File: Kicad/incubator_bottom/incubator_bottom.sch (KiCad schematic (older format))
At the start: 37 parts, among them J1 Conn_01x02, J2 Conn_02x03_Odd_Even, J3 RJ12, J4 Conn_01x05, J5 AudioJack3_SwitchTR, J6 AudioJack3_SwitchTR, J7 Conn_01x02, J8 Conn_01x06, Q1 ZXMS6004, Q2 IPB80N03S4L-03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

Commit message: fix: Power resistor size
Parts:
- removed H5, H6, H7, H8: MountingHole, MountingHole:MountingHole_4.3mm_M4, symbol incubator_bottom-rescue:MountingHole-Mechanical
- removed R7: HSC1004R0J, Incubator:HSC1004R0J, symbol Incubator:HSC1004R0J
- added R?: HSC1004R0J, Incubator:100W4RJ, symbol Incubator:HSC1004R0J
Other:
- note removed: "FAN HOLES"
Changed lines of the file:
@@
 NoConn ~ 7650 1475
-$Comp
-L incubator_bottom-rescue:MountingHole-Mechanical H5
-U 1 1 6110AD0D
-P 5025 7225
-F 0 "H5" H 5125 7271 50  0000 L CNN
-F 1 "MountingHole" H 5125 7180 50  0000 L CNN
-F 2 "MountingHole:MountingHole_4.3mm_M4" H 5025 7225 50  0001 C CNN
-F 3 "~" H 5025 7225 50  0001 C CNN
-	1    5025 7225
-	1    0    0    -1
-$EndComp
-$Comp
-L incubator_bottom-rescue:MountingHole-Mechanical H7
-U 1 1 6110B26F
-P 5800 7225
-F 0 "H7" H 5900 7271 50  0000 L CNN
-F 1 "MountingHole" H 5900 7180 50  0000 L CNN
-F 2 "MountingHole:MountingHole_4.3mm_M4" H 5800 7225 50  0001 C CNN
-F 3 "~" H 5800 7225 50  0001 C CNN
-	1    5800 7225
-	1    0    0    -1
-$EndComp
-$Comp
-L incubator_bottom-rescue:MountingHole-Mechanical H6
-U 1 1 6110B9C7
-P 5025 7500
-F 0 "H6" H 5125 7546 50  0000 L CNN
-F 1 "MountingHole" H 5125 7455 50  0000 L CNN
-F 2 "MountingHole:MountingHole_4.3mm_M4" H 5025 7500 50  0001 C CNN
-F 3 "~" H 5025 7500 50  0001 C CNN
-	1    5025 7500
-	1    0    0    -1
-$EndComp
-$Comp
-L incubator_bottom-rescue:MountingHole-Mechanical H8
-U 1 1 6110BE5B
-P 5800 7475
-F 0 "H8" H 5900 7521 50  0000 L CNN
-F 1 "MountingHole" H 5900 7430 50  0000 L CNN
-F 2 "MountingHole:MountingHole_4.3mm_M4" H 5800 7475 50  0001 C CNN
-F 3 "~" H 5800 7475 50  0001 C CNN
-	1    5800 7475
-	1    0    0    -1
-$EndComp
 $Comp
 L incubator_bottom-rescue:+12V-power #PWR0105
@@
 Text Notes 3600 7000 0    50   ~ 0
 EXTERNAL HOLES
-Text Notes 5500 7000 0    50   ~ 0
-FAN HOLES
 Text Notes 4675 6850 0    102  ~ 0
 HOLES
@@
 Wire Notes Line
 	475  3325 5925 3325
-$Comp
-L Incubator:HSC1004R0J R7
-U 1 1 610E9CE6
-P 8475 5300
-F 0 "R7" H 8545 5346 50  0000 L CNN
-F 1 "HSC1004R0J" H 8545 5255 50  0000 L CNN
-F 2 "Incubator:HSC1004R0J" V 8405 5300 50  0001 C CNN
-F 3 "https://www.mouser.com/datasheet/2/418/5/ENG_CD_1625999_AH2-1990035.pdf" H 8475 5300 50  0001 C CNN
-	1    8475 5300
-	1    0    0    -1
-$EndComp
-NoConn ~ 8475 5150
-NoConn ~ 8475 5450
+NoConn ~ 7700 5150
+NoConn ~ 7700 5450
 $Comp
 L incubator_bottom-rescue:C-Device C3
@@
 Text Notes 3250 5275 0    102  ~ 0
 PID
+$Comp
+L Incubator:HSC1004R0J R?
+U 1 1 6141DEAF
+P 7700 5300
+F 0 "R?" H 7770 5346 50  0000 L CNN
+F 1 "HSC1004R0J" H 7770 5255 50  0000 L CNN
+F 2 "Incubator:100W4RJ" V 7630 5300 50  0001 C CNN
+F 3 "https://www.mouser.com/datasheet/2/418/5/ENG_CD_1625999_AH2-1990035.pdf" H 7700 5300 50  0001 C CNN
+	1    7700 5300
+	1    0    0    -1
+$EndComp
 $EndSCHEMATC

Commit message: fix: Power resistor size and position
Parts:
- removed R?: HSC1004R0J, Incubator:100W4RJ, symbol Incubator:HSC1004R0J
- added R15, R7: 100W4RJ, Incubator:100W4RJ, symbol Incubator:HSC1004R0J
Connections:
- no-connect marks 8 -> 10
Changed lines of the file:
@@
 PID
 $Comp
-L Incubator:HSC1004R0J R?
-U 1 1 6141DEAF
+L Incubator:HSC1004R0J R15
+U 1 1 61434FDD
+P 6450 5250
+F 0 "R15" H 6520 5296 50  0000 L CNN
+F 1 "100W4RJ" H 6520 5205 50  0000 L CNN
+F 2 "Incubator:100W4RJ" V 6380 5250 50  0001 C CNN
+F 3 "https://www.mouser.com/datasheet/2/418/5/ENG_CD_1625999_AH2-1990035.pdf" H 6450 5250 50  0001 C CNN
+	1    6450 5250
+	1    0    0    -1
+$EndComp
+$Comp
+L Incubator:HSC1004R0J R7
+U 1 1 61442D39
 P 7700 5300
-F 0 "R?" H 7770 5346 50  0000 L CNN
-F 1 "HSC1004R0J" H 7770 5255 50  0000 L CNN
+F 0 "R7" H 7770 5346 50  0000 L CNN
+F 1 "100W4RJ" H 7770 5255 50  0000 L CNN
 F 2 "Incubator:100W4RJ" V 7630 5300 50  0001 C CNN
 F 3 "https://www.mouser.com/datasheet/2/418/5/ENG_CD_1625999_AH2-1990035.pdf" H 7700 5300 50  0001 C CNN
@@
 	1    0    0    -1
 $EndComp
+NoConn ~ 6450 5100
+NoConn ~ 6450 5400
 $EndSCHEMATC

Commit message: fix: fan connection
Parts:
- removed J4: Conn_01x05, Connector_PinHeader_2.54mm:PinHeader_1x05_P2.54mm_Vertical, symbol incubator_bottom-rescue:Conn_01x05-Connector_Generic
- removed R15: 100W4RJ, Incubator:100W4RJ, symbol Incubator:HSC1004R0J
- added H5, H6, H7, H8: MountingHole, MountingHole:MountingHole_3.2mm_M3, symbol incubator_bottom-rescue:MountingHole-Mechanical
- added J10, J11, J4, J9: Conn_01x01, Connector_Wire:SolderWirePad_1x01_SMD_5x10mm, symbol Connector_Generic:Conn_01x01
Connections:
- no-connect marks 10 -> 8
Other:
- note added: "FAN HOLES"
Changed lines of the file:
@@
 	1    0    0    -1
 $EndComp
-Text GLabel 4950 3925 0    50   Input ~ 0
+Text GLabel 4950 3900 0    50   Input ~ 0
 12V
-Wire Wire Line
-	5125 3925 5050 3925
-Wire Wire Line
-	5050 3925 5050 3850
 $Comp
 L incubator_bottom-rescue:GND-power #PWR0102
 U 1 1 611DACB0
-P 5050 4400
-F 0 "#PWR0102" H 5050 4150 50  0001 C CNN
-F 1 "GND" H 5055 4227 50  0000 C CNN
-F 2 "" H 5050 4400 50  0001 C CNN
-F 3 "" H 5050 4400 50  0001 C CNN
-	1    5050 4400
-	1    0    0    -1
-$EndComp
-Wire Wire Line
-	5125 4125 5050 4125
-Wire Wire Line
-	5050 4125 5050 4400
-Text GLabel 4950 4225 0    50   Input ~ 0
+P 5050 4450
+F 0 "#PWR0102" H 5050 4200 50  0001 C CNN
+F 1 "GND" H 5055 4277 50  0000 C CNN
+F 2 "" H 5050 4450 50  0001 C CNN
+F 3 "" H 5050 4450 50  0001 C CNN
+	1    5050 4450
+	1    0    0    -1
+$EndComp
+Text GLabel 4950 4200 0    50   Input ~ 0
 SDA
-Text GLabel 4950 4325 0    50   Input ~ 0
+Text GLabel 4950 4350 0    50   Input ~ 0
 SCL
-Wire Wire Line
-	5125 4325 4950 4325
-Wire Wire Line
-	4950 4225 5125 4225
 $Comp
 L incubator_bottom-rescue:AudioJack3_SwitchTR-Connector J5
@@
 L incubator_bottom-rescue:+12V-power #PWR0105
 U 1 1 6111A394
-P 5050 3850
-F 0 "#PWR0105" H 5050 3700 50  0001 C CNN
-F 1 "+12V" H 5065 4023 50  0000 C CNN
-F 2 "" H 5050 3850 50  0001 C CNN
-F 3 "" H 5050 3850 50  0001 C CNN
-	1    5050 3850
-	1    0    0    -1
-$EndComp
-Wire Wire Line
-	4950 3925 5050 3925
-Connection ~ 5050 3925
+P 5050 3800
+F 0 "#PWR0105" H 5050 3650 50  0001 C CNN
+F 1 "+12V" H 5065 3973 50  0000 C CNN
+F 2 "" H 5050 3800 50  0001 C CNN
+F 3 "" H 5050 3800 50  0001 C CNN
+	1    5050 3800
+	1    0    0    -1
+$EndComp
 $Comp
 L incubator_bottom-rescue:+12V-power #PWR0108
@@
 Text Notes 1950 5250 0    102  ~ 0
 FAN
-$Comp
-L incubator_bottom-rescue:Conn_01x05-Connector_Generic J4
-U 1 1 6118C3B2
-P 5325 4125
-F 0 "J4" H 5405 4167 50  0000 L CNN
-F 1 "Conn_01x05" H 5405 4076 50  0000 L CNN
-F 2 "Connector_PinHeader_2.54mm:PinHeader_1x05_P2.54mm_Vertical" H 5325 4125 50  0001 C CNN
-F 3 "~" H 5325 4125 50  0001 C CNN
-	1    5325 4125
-	1    0    0    -1
-$EndComp
 Text GLabel 4750 1025 2    50   Input ~ 0
 C0
@@
 PID
 $Comp
-L Incubator:HSC1004R0J R15
-U 1 1 61434FDD
-P 6450 5250
-F 0 "R15" H 6520 5296 50  0000 L CNN
-F 1 "100W4RJ" H 6520 5205 50  0000 L CNN
-F 2 "Incubator:100W4RJ" V 6380 5250 50  0001 C CNN
-F 3 "https://www.mouser.com/datasheet/2/418/5/ENG_CD_1625999_AH2-1990035.pdf" H 6450 5250 50  0001 C CNN
-	1    6450 5250
-	1    0    0    -1
-$EndComp
-$Comp
 L Incubator:HSC1004R0J R7
 U 1 1 61442D39
@@
 	1    0    0    -1
 $EndComp
-NoConn ~ 6450 5100
-NoConn ~ 6450 5400
+$Comp
+L Connector_Generic:Conn_01x01 J4
+U 1 1 61426717
+P 5350 3900
+F 0 "J4" H 5430 3942 50  0000 L CNN
+F 1 "Conn_01x01" H 5430 3851 50  0000 L CNN
+F 2 "Connector_Wire:SolderWirePad_1x01_SMD_5x10mm" H 5350 3900 50  0001 C CNN
+F 3 "~" H 5350 3900 50  0001 C CNN
+	1    5350 3900
+	1    0    0    -1
+$EndComp
+$Comp
+L Connector_Generic:Conn_01x01 J11
+U 1 1 614274D6
+P 5350 4350
+F 0 "J11" H 5430 4392 50  0000 L CNN
+F 1 "Conn_01x01" H 5430 4301 50  0000 L CNN
+F 2 "Connector_Wire:SolderWirePad_1x01_SMD_5x10mm" H 5350 4350 50  0001 C CNN
+F 3 "~" H 5350 4350 50  0001 C CNN
+	1    5350 4350
+	1    0    0    -1
+$EndComp
+Wire Wire Line
+	4950 3900 5050 3900
+Wire Wire Line
+	5050 3800 5050 3900
+Connection ~ 5050 3900
+Wire Wire Line
+	5050 3900 5150 3900
+Wire Wire Line
+	5150 4050 5050 4050
+$Comp
+L Connector_Generic:Conn_01x01 J10
+U 1 1 61427056
+P 5350 4200
+F 0 "J10" H 5430 4242 50  0000 L CNN
+F 1 "Conn_01x01" H 5430 4151 50  0000 L CNN
+F 2 "Connector_Wire:SolderWirePad_1x01_SMD_5x10mm" H 5350 4200 50  0001 C CNN
+F 3 "~" H 5350 4200 50  0001 C CNN
+	1    5350 4200
+	1    0    0    -1
+$EndComp
+$Comp
+L Connector_Generic:Conn_01x01 J9
+U 1 1 61426C44
+P 5350 4050
+F 0 "J9" H 5430 4092 50  0000 L CNN
+F 1 "Conn_01x01" H 5430 4001 50  0000 L CNN
+F 2 "Connector_Wire:SolderWirePad_1x01_SMD_5x10mm" H 5350 4050 50  0001 C CNN
+F 3 "~" H 5350 4050 50  0001 C CNN
+	1    5350 4050
+	1    0    0    -1
+$EndComp
+Wire Wire Line
+	5050 4450 5050 4050
+Wire Wire Line
+	4950 4200 5150 4200
+Wire Wire Line
+	5150 4350 4950 4350
+$Comp
+L incubator_bottom-rescue:MountingHole-Mechanical H5
+U 1 1 614A8308
+P 5000 7150
+F 0 "H5" H 5100 7196 50  0000 L CNN
+F 1 "MountingHole" H 5100 7105 50  0000 L CNN
+F 2 "MountingHole:MountingHole_3.2mm_M3" H 5000 7150 50  0001 C CNN
+F 3 "~" H 5000 7150 50  0001 C CNN
+	1    5000 7150
+	1    0    0    -1
+$EndComp
+$Comp
+L incubator_bottom-rescue:MountingHole-Mechanical H6
+U 1 1 614A89BD
+P 5000 7450
+F 0 "H6" H 5100 7496 50  0000 L CNN
+F 1 "MountingHole" H 5100 7405 50  0000 L CNN
+F 2 "MountingHole:MountingHole_3.2mm_M3" H 5000 7450 50  0001 C CNN
+F 3 "~" H 5000 7450 50  0001 C CNN
+	1    5000 7450
+	1    0    0    -1
+$EndComp
+$Comp
+L incubator_bottom-rescue:MountingHole-Mechanical H7
+U 1 1 614A8DD5
+P 5800 7150
+F 0 "H7" H 5900 7196 50  0000 L CNN
+F 1 "MountingHole" H 5900 7105 50  0000 L CNN
+F 2 "MountingHole:MountingHole_3.2mm_M3" H 5800 7150 50  0001 C CNN
+F 3 "~" H 5800 7150 50  0001 C CNN
+	1    5800 7150
+	1    0    0    -1
+$EndComp
+$Comp
+L incubator_bottom-rescue:MountingHole-Mechanical H8
+U 1 1 614A963E
+P 5800 7450
+F 0 "H8" H 5900 7496 50  0000 L CNN
+F 1 "MountingHole" H 5900 7405 50  0000 L CNN
+F 2 "MountingHole:MountingHole_3.2mm_M3" H 5800 7450 50  0001 C CNN
+F 3 "~" H 5800 7450 50  0001 C CNN
+	1    5800 7450
+	1    0    0    -1
+$EndComp
+Text Notes 5250 7000 0    50   ~ 0
+FAN HOLES
 $EndSCHEMATC

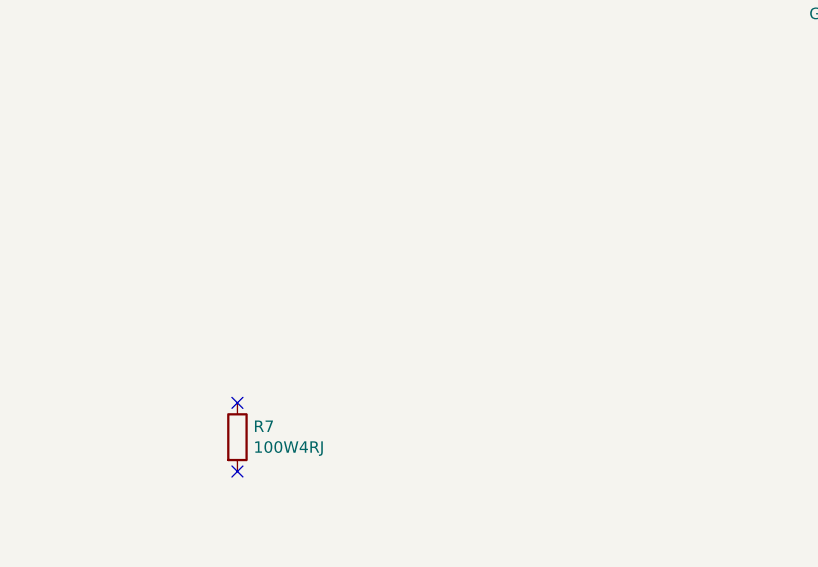
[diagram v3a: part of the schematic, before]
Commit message: refactor:Step-down IC was changed
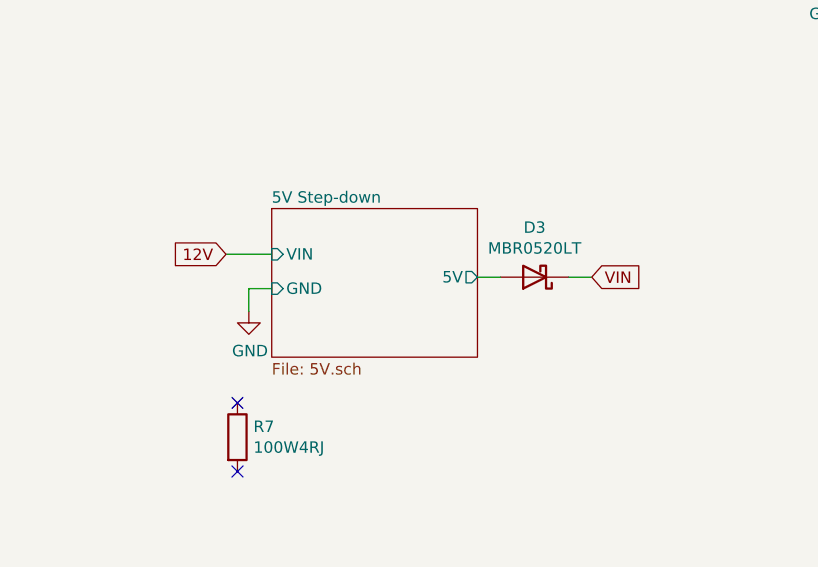
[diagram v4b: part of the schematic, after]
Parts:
- added D3: MBR0520LT, Diode_SMD:D_SOD-123, symbol incubator_bottom-rescue:MBR0520LT-Diode
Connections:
- net VIN: now also D3.1 (K)
- new net 5V Step-down/5V: D3.2 (A)
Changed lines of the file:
@@
 $Descr A4 11693 8268
 encoding utf-8
-Sheet 1 2
+Sheet 1 3
 Title ""
 Date ""
@@
 Text Notes 5250 7000 0    50   ~ 0
 FAN HOLES
+$Sheet
+S 7850 4300 900  650
+U 61425B26
+F0 "5V Step-down" 50
+F1 "5V.sch" 50
+F2 "VIN" I L 7850 4500 50
+F3 "5V" O R 8750 4600 50
+F4 "GND" I L 7850 4650 50
+$EndSheet
+Text GLabel 7650 4500 0    50   Input ~ 0
+12V
+$Comp
+L incubator_bottom-rescue:GND-power #PWR01
+U 1 1 61433F4F
+P 7750 4750
+F 0 "#PWR01" H 7750 4500 50  0001 C CNN
+F 1 "GND" H 7755 4577 50  0000 C CNN
+F 2 "" H 7750 4750 50  0001 C CNN
+F 3 "" H 7750 4750 50  0001 C CNN
+	1    7750 4750
+	1    0    0    -1
+$EndComp
+Wire Wire Line
+	7750 4750 7750 4650
+Wire Wire Line
+	7750 4650 7850 4650
+Wire Wire Line
+	7850 4500 7650 4500
+Text GLabel 9250 4600 2    50   Input ~ 0
+VIN
+$Comp
+L incubator_bottom-rescue:MBR0520LT-Diode D3
+U 1 1 61445FAB
+P 9000 4600
+F 0 "D3" H 9000 4383 50  0000 C CNN
+F 1 "MBR0520LT" H 9000 4474 50  0000 C CNN
+F 2 "Diode_SMD:D_SOD-123" H 9000 4425 50  0001 C CNN
+F 3 "http://www.onsemi.com/pub_link/Collateral/MBR0520LT1-D.PDF" H 9000 4600 50  0001 C CNN
+	1    9000 4600
+	-1   0    0    1
+$EndComp
+Wire Wire Line
+	9250 4600 9150 4600
+Wire Wire Line
+	8850 4600 8750 4600
 $EndSCHEMATC

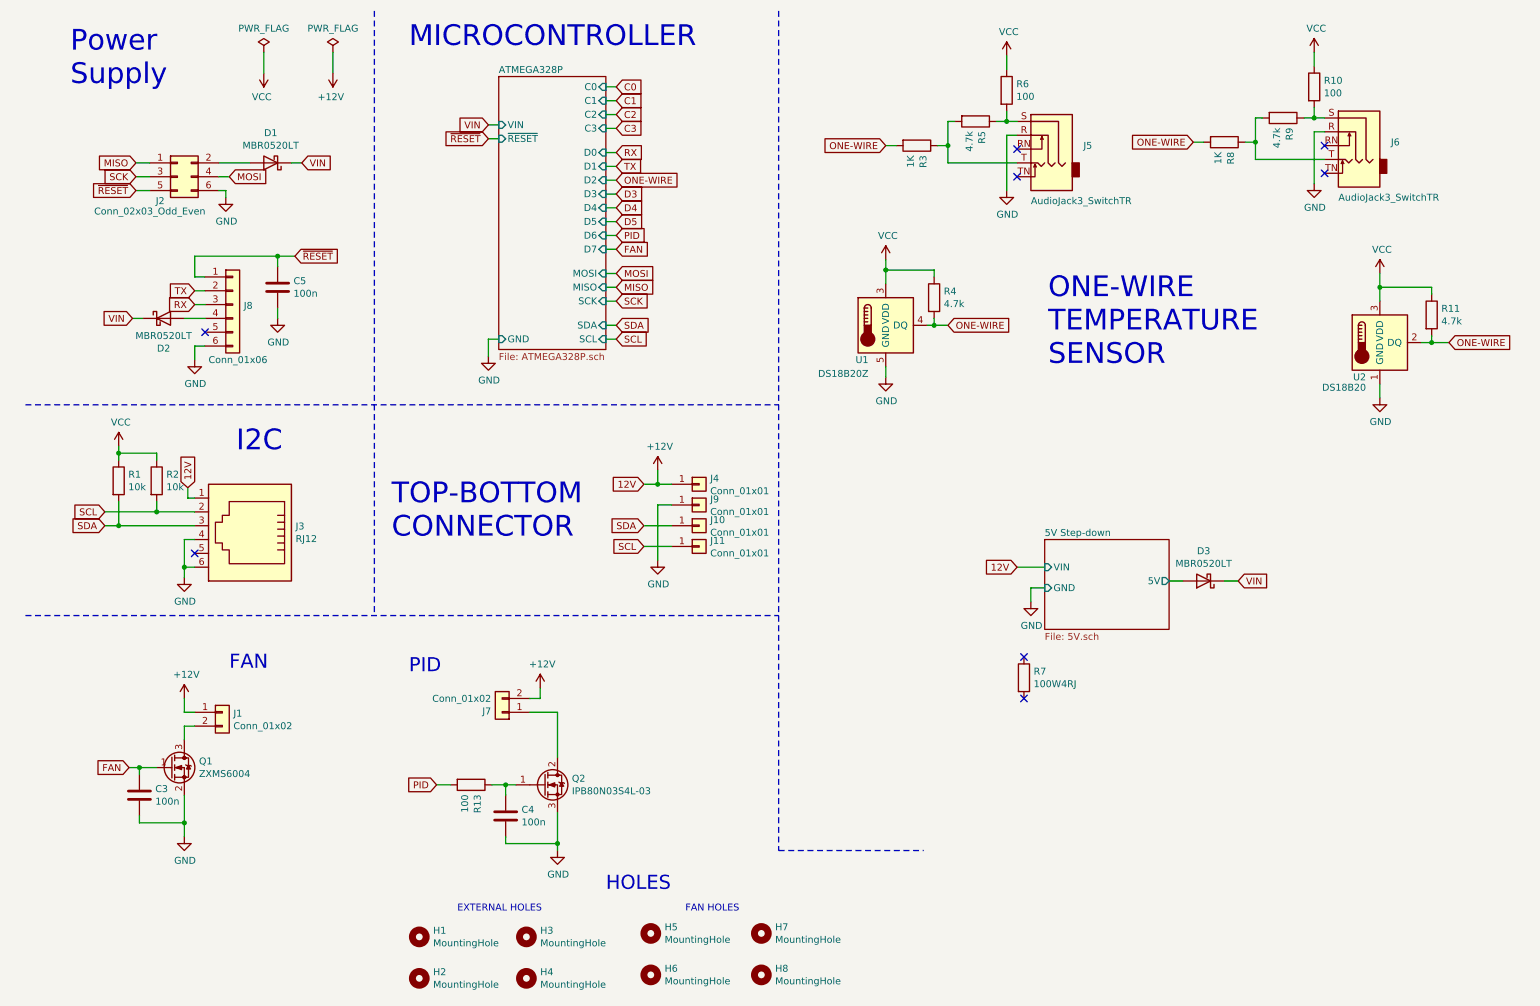
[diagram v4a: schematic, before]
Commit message: fix: Routes and positions for Power resistor, 5V Step-down and uC were changed
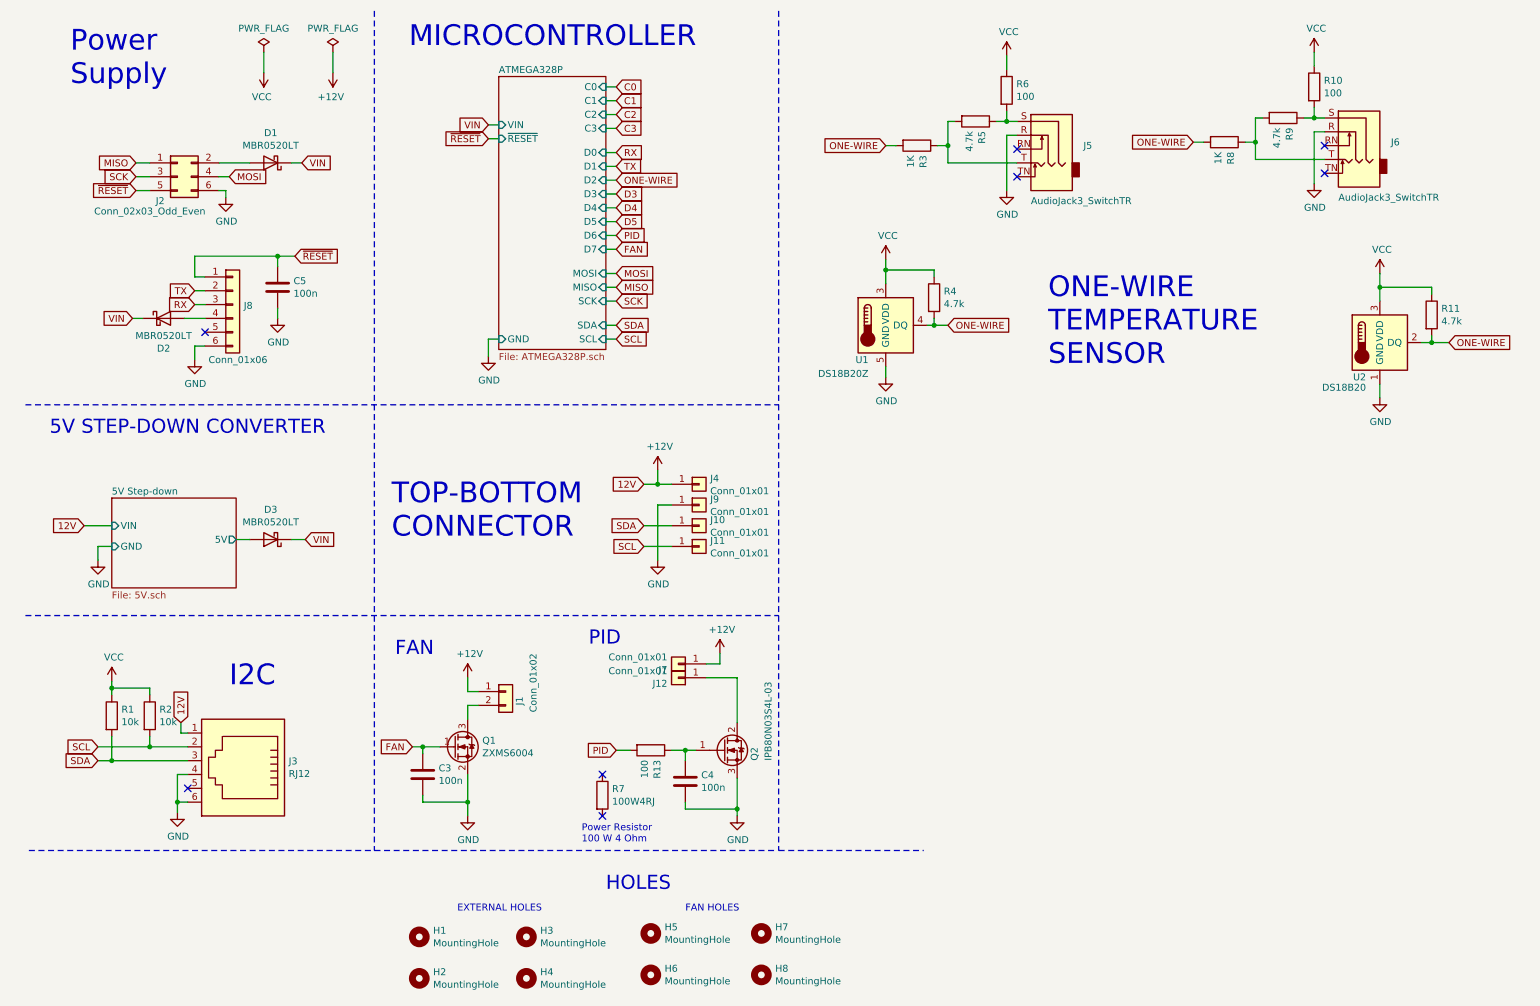
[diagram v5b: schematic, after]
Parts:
- removed J7: Conn_01x02, Connector_JST:JST_XH_B2B-XH-A_1x02_P2.50mm_Vertical, symbol incubator_bottom-rescue:Conn_01x02-Connector_Generic
- added J12, J7: Conn_01x01, Connector_Wire:SolderWirePad_1x01_SMD_5x10mm, symbol Connector_Generic:Conn_01x01
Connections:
- net +12V: now also J7.1 (Pin_1)
- net at Q2.2 (D): now also J12.1 (Pin_1)
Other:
- note added: "5V STEP-DOWN CONVERTER"
- note added: "Power Resistor\n100 W 4 Ohm"
- moved on the sheet: C3, C4, D3, J1, J3, Q1, Q2, R1, R13, R2, R7
